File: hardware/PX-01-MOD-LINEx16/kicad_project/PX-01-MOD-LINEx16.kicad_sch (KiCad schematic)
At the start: 50 parts, among them J8 Conn_01x07_Socket, J9 Conn_01x08

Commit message: Añade Revisión y Modelos 3D
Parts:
- C1, C2, C3, C4: footprint (none) -> Capacitor_SMD:C_0805_2012Metric_Pad1.18x1.45mm_HandSolder

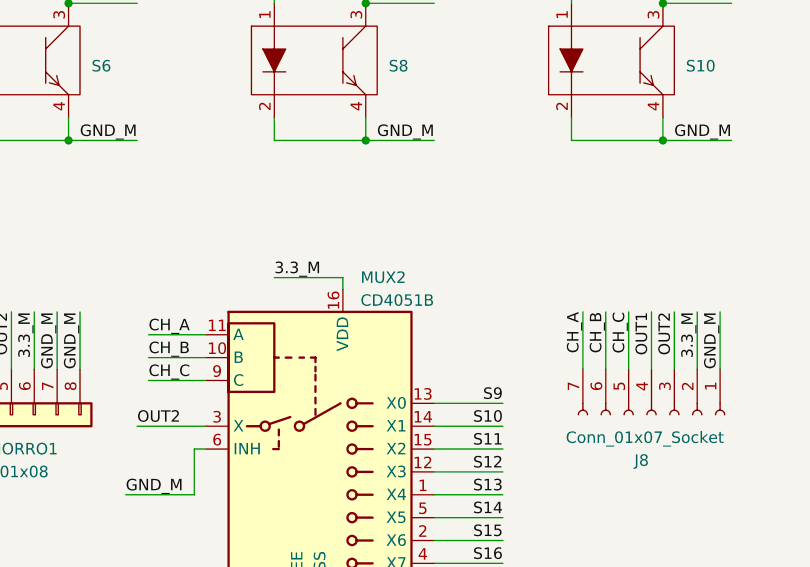
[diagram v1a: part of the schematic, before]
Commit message: Actualiza Silkscreen para PCB en negro y añade referencias LCSC
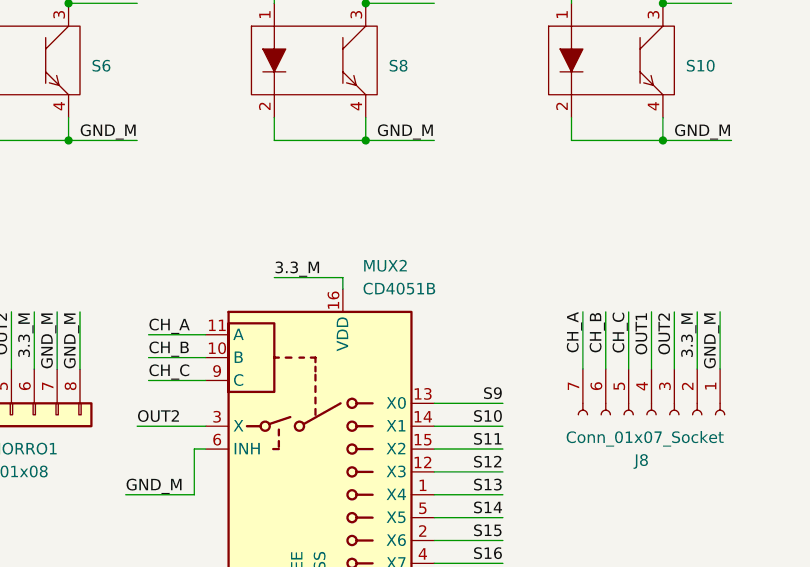
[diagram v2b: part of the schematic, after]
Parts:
- AUX_FLEX1, FLEX_MORRO1: footprint custom_footprints:TE_0-1734839-8_1x08-1MP_P0.5mm_Horizontal -> custom_footprints:FPC0.5-8P; LCSC Part # (none) -> C388694
- C1, C3: LCSC Part # (none) -> C109040
- C2, C4: LCSC Part # (none) -> C2847428
- J8, J9: now left out of the parts list
- MUX1, MUX2: footprint Package_SO:TSSOP-16_4.4x5mm_P0.65mm -> custom_footprints:MUX_CD4051B; symbol Analog_Switch:CD4051B -> custom_symbols:MUX_CD4051B; JLCPCB Rotation Offset (none) -> 90; LCSC Part # (none) -> C3007951
- R1, R10, R13, R16, R19, R22, R4, R7: LCSC Part # (none) -> C3017827
- R11, R12, R14, R15, R17, R18, R2, R20, R21, R23, R24, R3, R5, R6, R8, R9: LCSC Part # (none) -> C3016736
- S1, S10, S11, S12, S13, S14, S15, S16, S2, S3, S4, S5, S6, S7, S8, S9: footprint custom_footprints:QRE1113_fujitora -> custom_footprints:ITR8307_SMD; symbol custom_symbols:QRE1113 -> custom_symbols:ITR8307_SMD; JLCPCB Rotation Offset (none) -> 180; LCSC Part # (none) -> C81632

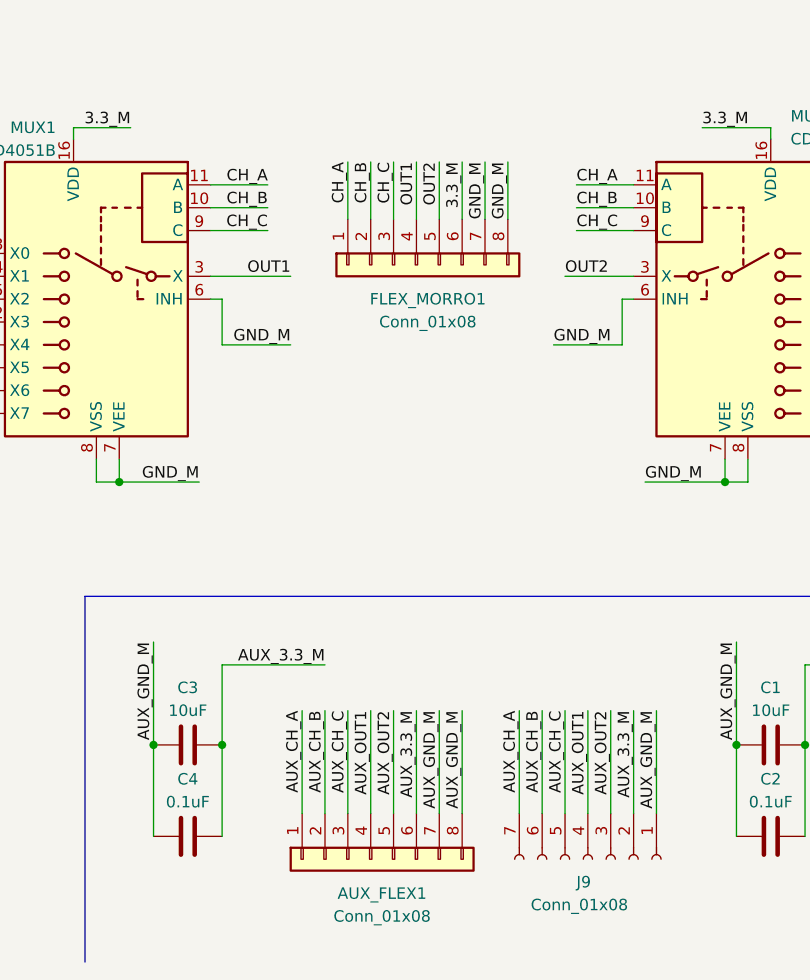
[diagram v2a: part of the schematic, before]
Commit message: Añade gerbers y actualiza flex a 7P. Cambia la referencia de algunos componentes
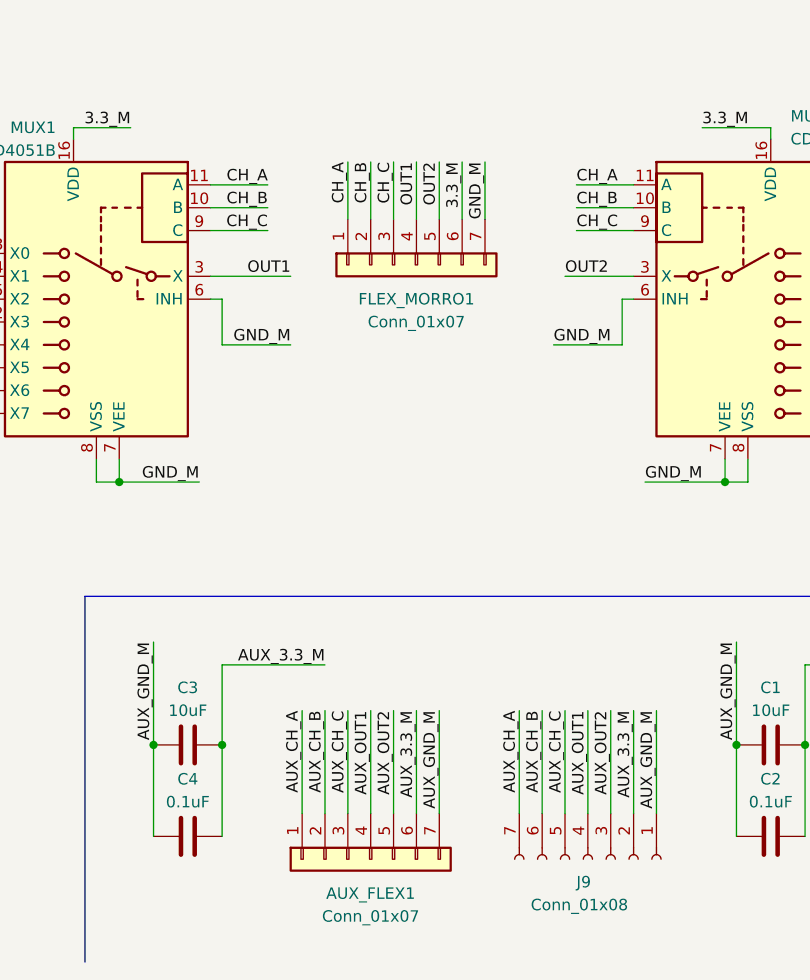
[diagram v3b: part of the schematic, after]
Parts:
- AUX_FLEX1, FLEX_MORRO1: value Conn_01x08 -> Conn_01x07; footprint custom_footprints:FPC0.5-8P -> Connector_FFC-FPC:TE_0-1734839-7_1x07-1MP_P0.5mm_Horizontal; symbol Connector_Generic:Conn_01x08 -> Connector_Generic:Conn_01x07; JLCPCB Position Offset (none) -> 0,-0.4; LCSC Part # C388694 -> C388693
- C1, C3: LCSC Part # C109040 -> C380331
- R11, R12, R14, R15, R17, R18, R2, R20, R21, R23, R24, R3, R5, R6, R8, R9: LCSC Part # C3016736 -> C17414
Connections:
- net AUX_GND_M: no longer AUX_FLEX1.8 (Pin_8)
- net GND_M: no longer FLEX_MORRO1.8 (Pin_8)
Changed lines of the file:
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@@
-    (stroke (width 0) (type default))
-  )
-  (wire (pts (xy 101.6 109.22) (xy 101.6 115.57))
     (stroke (width 0) (type default))
   )
@@
   )
   (wire (pts (xy 100.33 90.17) (xy 100.33 87.63))
-    (stroke (width 0) (type default))
-  )
-  (wire (pts (xy 96.52 170.18) (xy 96.52 181.61))
     (stroke (width 0) (type default))
   )
@@
     (effects (font (size 1.27 1.27)) (justify right bottom))
   )
-  (label "AUX_GND_M" (at 96.52 170.18 270) (fields_autoplaced)
-    (effects (font (size 1.27 1.27)) (justify right bottom))
-  )
   (label "AUX_CH_B" (at 81.28 170.18 270) (fields_autoplaced)
     (effects (font (size 1.27 1.27)) (justify right bottom))
@@
   (label "CH_B" (at 109.22 114.3 0) (fields_autoplaced)
     (effects (font (size 1.27 1.27)) (justify left bottom))
-  )
-  (label "GND_M" (at 101.6 109.22 270) (fields_autoplaced)
-    (effects (font (size 1.27 1.27)) (justify right bottom))
   )
   (label "3.3_M" (at 34.29 48.26 180) (fields_autoplaced)
@@
       (effects (font (size 1.27 1.27)) hide)
     )
-    (property "LCSC Part #" "C3016736" (at 104.14 69.85 90)
+    (property "LCSC Part #" "C17414" (at 104.14 69.85 90)
       (effects (font (size 1.27 1.27)) hide)
     )
@@
       (effects (font (size 1.27 1.27)) hide)
     )
-    (property "LCSC Part #" "C3016736" (at 43.18 46.99 0)
+    (property "LCSC Part #" "C17414" (at 43.18 46.99 0)
       (effects (font (size 1.27 1.27)) hide)
     )
@@
       (effects (font (size 1.27 1.27)) hide)
     )
-    (property "LCSC Part #" "C3016736" (at 104.14 46.99 90)
+    (property "LCSC Part #" "C17414" (at 104.14 46.99 90)
       (effects (font (size 1.27 1.27)) hide)
     )
@@
       (effects (font (size 1.27 1.27)) hide)
     )
-    (property "LCSC Part #" "C3016736" (at 264.16 46.99 90)
+    (property "LCSC Part #" "C17414" (at 264.16 46.99 90)
       (effects (font (size 1.27 1.27)) hide)
     )
@@
     )
   )
-  (symbol (lib_id "Connector_Generic:Conn_01x08") (at 86.36 186.69 90) (mirror x) (unit 1)
+  (symbol (lib_id "Connector_Generic:Conn_01x07") (at 86.36 186.69 90) (mirror x) (unit 1)
     (in_bom yes) (on_board yes) (dnp no)
-    (property "Reference" "AUX_FLEX1" (at 87.63 190.5 90)
-      (effects (font (size 1.27 1.27)))
-    )
-    (property "Value" "Conn_01x08" (at 87.63 193.04 90)
-      (effects (font (size 1.27 1.27)))
-    )
-    (property "Footprint" "custom_footprints:FPC0.5-8P" (at 86.36 186.69 0)
+    (property "Reference" "AUX_FLEX1" (at 86.36 190.5 90)
+      (effects (font (size 1.27 1.27)))
+    )
+    (property "Value" "Conn_01x07" (at 86.36 193.04 90)
+      (effects (font (size 1.27 1.27)))
+    )
+    (property "Footprint" "Connector_FFC-FPC:TE_0-1734839-7_1x07-1MP_P0.5mm_Horizontal" (at 86.36 186.69 0)
       (effects (font (size 1.27 1.27)) hide)
     )
@@
       (effects (font (size 1.27 1.27)) hide)
     )
-    (property "LCSC Part #" "C388694" (at 86.36 186.69 90)
+    (property "LCSC Part #" "C388693" (at 86.36 186.69 90)
+      (effects (font (size 1.27 1.27)) hide)
+    )
+    (property "JLCPCB Position Offset" "0,-0.4" (at 86.36 186.69 90)
       (effects (font (size 1.27 1.27)) hide)
     )
@@
     (pin "6")
     (pin "7")
-    (pin "8")
     (instances
       (project "PX-01-MOD-LINEx16"
@@
       (effects (font (size 1.27 1.27)) hide)
     )
-    (property "LCSC Part #" "C3016736" (at 137.16 46.99 90)
+    (property "LCSC Part #" "C17414" (at 137.16 46.99 90)
       (effects (font (size 1.27 1.27)) hide)
     )
@@
       (effects (font (size 1.27 1.27)) hide)
     )
-    (property "LCSC Part #" "C3016736" (at 43.18 69.85 90)
+    (property "LCSC Part #" "C17414" (at 43.18 69.85 90)
       (effects (font (size 1.27 1.27)) hide)
     )
@@
       (effects (font (size 1.27 1.27)) hide)
     )
-    (property "LCSC Part #" "C3016736" (at 232.41 69.85 90)
+    (property "LCSC Part #" "C17414" (at 232.41 69.85 90)
       (effects (font (size 1.27 1.27)) hide)
     )
@@
       (effects (font (size 1.27 1.27)) hide)
     )
-    (property "LCSC Part #" "C3016736" (at 264.16 69.85 90)
+    (property "LCSC Part #" "C17414" (at 264.16 69.85 90)
       (effects (font (size 1.27 1.27)) hide)
     )
@@
       (effects (font (size 1.27 1.27)) hide)
     )
-    (property "LCSC Part #" "C3016736" (at 170.18 69.85 90)
+    (property "LCSC Part #" "C17414" (at 170.18 69.85 90)
       (effects (font (size 1.27 1.27)) hide)
     )
@@
       (effects (font (size 1.27 1.27)) hide)
     )
-    (property "LCSC Part #" "C3016736" (at 232.41 46.99 90)
+    (property "LCSC Part #" "C17414" (at 232.41 46.99 90)
       (effects (font (size 1.27 1.27)) hide)
     )
@@
     )
   )
-  (symbol (lib_id "Connector_Generic:Conn_01x08") (at 91.44 120.65 90) (mirror x) (unit 1)
+  (symbol (lib_id "Connector_Generic:Conn_01x07") (at 91.44 120.65 90) (mirror x) (unit 1)
     (in_bom yes) (on_board yes) (dnp no)
-    (property "Reference" "FLEX_MORRO1" (at 92.71 124.46 90)
-      (effects (font (size 1.27 1.27)))
-    )
-    (property "Value" "Conn_01x08" (at 92.71 127 90)
-      (effects (font (size 1.27 1.27)))
-    )
-    (property "Footprint" "custom_footprints:FPC0.5-8P" (at 91.44 120.65 0)
+    (property "Reference" "FLEX_MORRO1" (at 91.44 124.46 90)
+      (effects (font (size 1.27 1.27)))
+    )
+    (property "Value" "Conn_01x07" (at 91.44 127 90)
+      (effects (font (size 1.27 1.27)))
+    )
+    (property "Footprint" "Connector_FFC-FPC:TE_0-1734839-7_1x07-1MP_P0.5mm_Horizontal" (at 91.44 120.65 0)
       (effects (font (size 1.27 1.27)) hide)
     )
@@
       (effects (font (size 1.27 1.27)) hide)
     )
-    (property "LCSC Part #" "C388694" (at 91.44 120.65 90)
+    (property "LCSC Part #" "C388693" (at 91.44 120.65 90)
+      (effects (font (size 1.27 1.27)) hide)
+    )
+    (property "JLCPCB Position Offset" "0,-0.4" (at 91.44 120.65 90)
       (effects (font (size 1.27 1.27)) hide)
     )
@@
     (pin "6")
     (pin "7")
-    (pin "8")
     (instances
       (project "PX-01-MOD-LINEx16"
@@
       (effects (font (size 1.27 1.27)) hide)
     )
-    (property "LCSC Part #" "C3016736" (at 73.66 46.99 90)
+    (property "LCSC Part #" "C17414" (at 73.66 46.99 90)
       (effects (font (size 1.27 1.27)) hide)
     )
@@
       (effects (font (size 1.27 1.27)) hide)
     )
-    (property "LCSC Part #" "C109040" (at 66.04 173.99 90)
+    (property "LCSC Part #" "C380331" (at 66.04 173.99 90)
       (effects (font (size 1.27 1.27)) hide)
     )
@@
       (effects (font (size 1.27 1.27)) hide)
     )
-    (property "LCSC Part #" "C109040" (at 130.81 173.99 90)
+    (property "LCSC Part #" "C380331" (at 130.81 173.99 90)
       (effects (font (size 1.27 1.27)) hide)
     )
@@
       (effects (font (size 1.27 1.27)) hide)
     )
-    (property "LCSC Part #" "C3016736" (at 170.18 46.99 90)
+    (property "LCSC Part #" "C17414" (at 170.18 46.99 90)
       (effects (font (size 1.27 1.27)) hide)
     )
@@
       (effects (font (size 1.27 1.27)) hide)
     )
-    (property "LCSC Part #" "C3016736" (at 201.93 69.85 90)
+    (property "LCSC Part #" "C17414" (at 201.93 69.85 90)
       (effects (font (size 1.27 1.27)) hide)
     )
@@
       (effects (font (size 1.27 1.27)) hide)
     )
-    (property "LCSC Part #" "C3016736" (at 201.93 46.99 90)
+    (property "LCSC Part #" "C17414" (at 201.93 46.99 90)
       (effects (font (size 1.27 1.27)) hide)
     )
@@
       (effects (font (size 1.27 1.27)) hide)
     )
-    (property "LCSC Part #" "C3016736" (at 137.16 69.85 90)
+    (property "LCSC Part #" "C17414" (at 137.16 69.85 90)
       (effects (font (size 1.27 1.27)) hide)
     )
@@
       (effects (font (size 1.27 1.27)) hide)
     )
-    (property "LCSC Part #" "C3016736" (at 73.66 69.85 90)
-      (effects (font (size 1.27 1.27)) hide)
-    )
+    (property "LCSC Part #" "C17414" (at 73.66 69.85 90)
+      (effects (font (size 1.27 1.27)) hide)
+    )
